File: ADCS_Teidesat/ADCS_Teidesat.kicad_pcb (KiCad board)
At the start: 2 copper layers, 90.2 x 95.9 mm, 10 parts

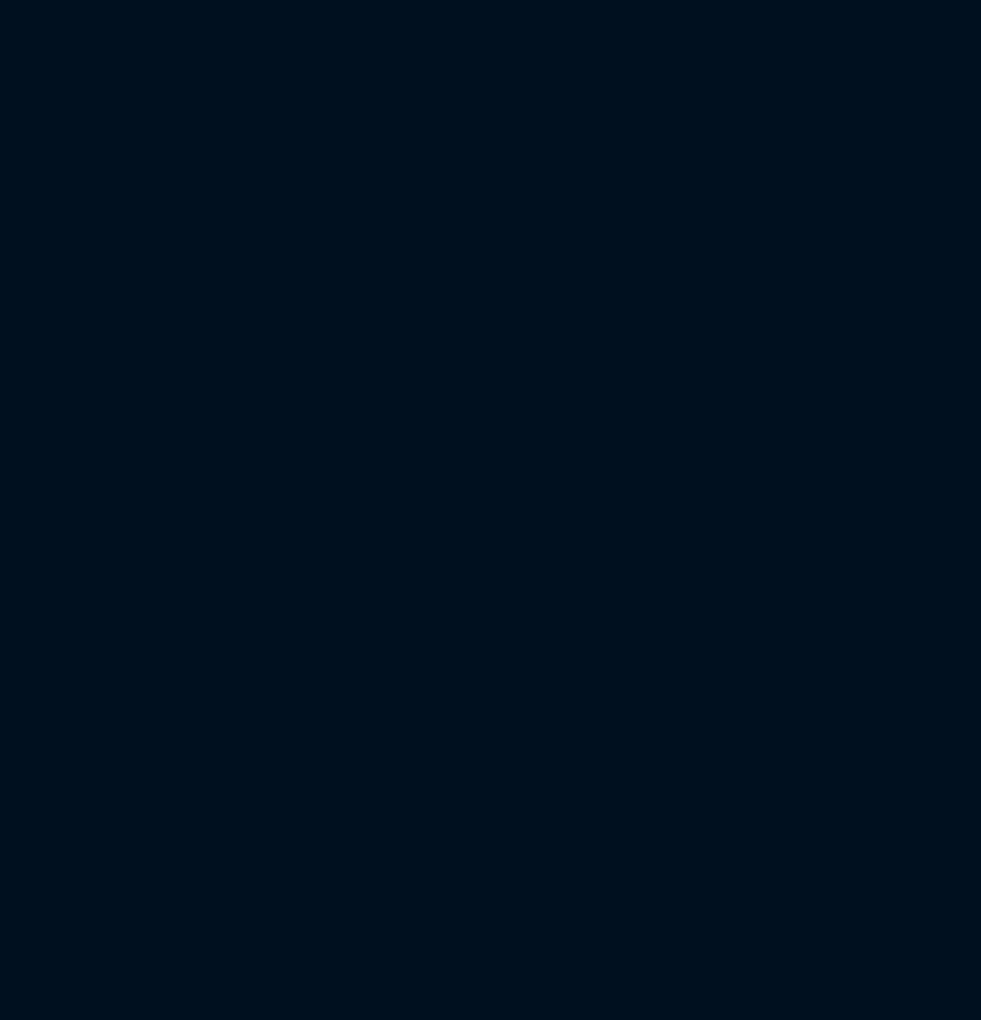
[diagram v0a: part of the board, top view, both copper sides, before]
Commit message: Comienzo PCB
Realizamos los últimos arreglos en las huellas de los componentes y comenzamos el diseño de la PCB

Co-Authored-By: hugohdezmo <238262256+hugohdezmo@users.noreply.github.com>
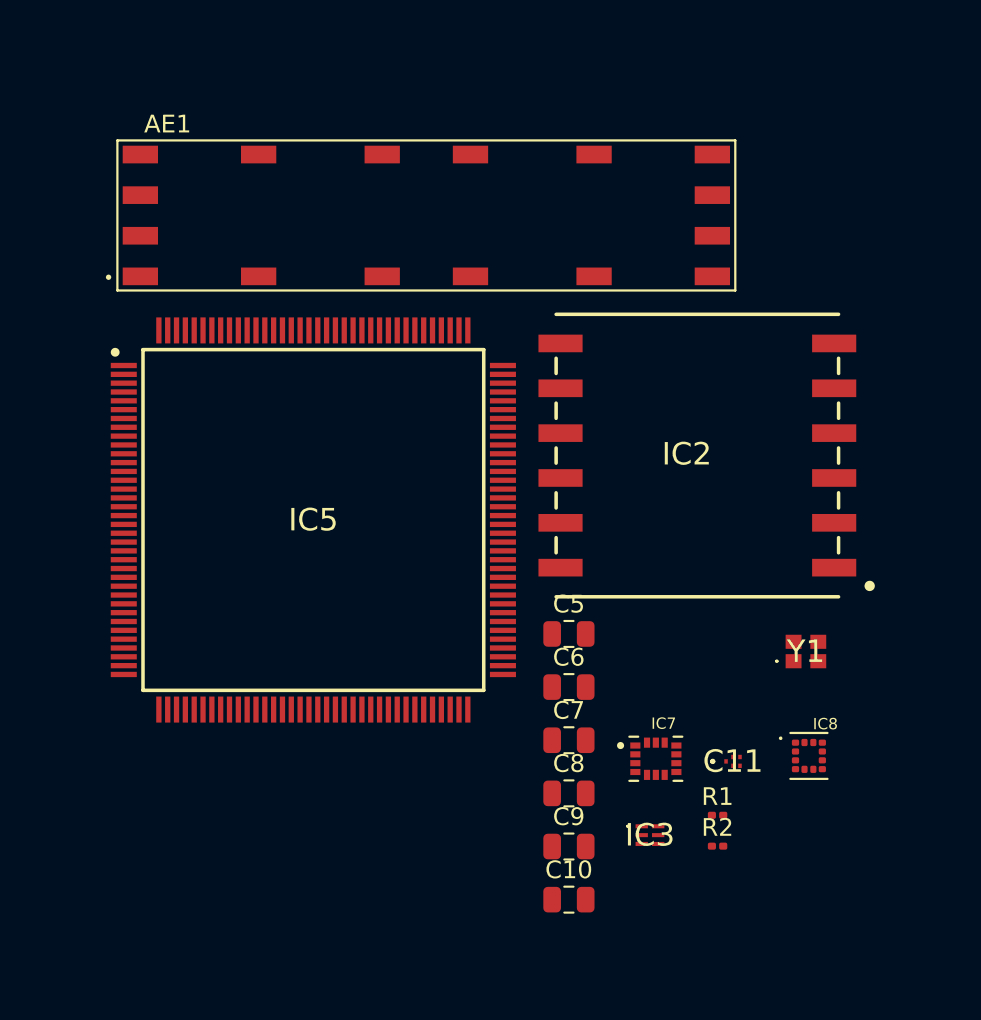
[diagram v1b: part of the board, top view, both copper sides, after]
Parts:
- added AE1: SR4L002, Huellas ADCS:XCVR_SR4L002, F.Cu at (142.1, 83.1)
- added C10: 100n, Capacitor_SMD:C_0805_2012Metric, F.Cu at (150.1, 121.9)
- added C11: F6QA1G581M2QZ-J, Huellas ADCS:F6QA1G581M2QZJ, F.Cu at (159.4, 114.1)
- added C5: 100n, Capacitor_SMD:C_0805_2012Metric, F.Cu at (150.1, 106.8)
- added C6: 100n, Capacitor_SMD:C_0805_2012Metric, F.Cu at (150.1, 109.9)
- added C7: 100n, Capacitor_SMD:C_0805_2012Metric, F.Cu at (150.1, 112.9)
- added C8: 220n, Capacitor_SMD:C_0805_2012Metric, F.Cu at (150.1, 115.9)
- added C9: 100n, Capacitor_SMD:C_0805_2012Metric, F.Cu at (150.1, 118.9)
- added IC2: L86-M33, Huellas ADCS:L80-M39, F.Cu at (149.7, 91.7)
- added IC3: MAX2659ELT+T, Huellas ADCS:MAX2659ELTT, F.Cu at (154.7, 118.2)
- added IC5: TMS5703137DPGEQQ1, Huellas ADCS:QFP50P2200X2200X160-144N, F.Cu at (135.7, 100.4)
- added IC7: LSM6DSV16XTR, Huellas ADCS:XDCR_LSM6DSV16XTR, F.Cu at (155.1, 113.9)
- added IC8: LIS2MDLTR, Huellas ADCS:PQFN50P200X200X70-12N, F.Cu at (163.7, 113.8)
- added R1: 10k, Resistor_SMD:R_0201_0603Metric, F.Cu at (158.6, 117.1)
- added R2: 10k, Resistor_SMD:R_0201_0603Metric, F.Cu at (158.6, 118.9)
- added Y1: ATX-H13-F-16.000MHz-G100-T, Huellas ADCS:ATXH13F16000MHzG100T, F.Cu at (163.6, 107.8)
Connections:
- H1 pad 11: TX2/GP8 -> unconnected-(H1-Pin_11-Pad11)
- H1 pad 13: GP15/A1/RX3 -> unconnected-(H1-Pin_13-Pad13)
- H1 pad 17: GP21/A7/RX5 -> unconnected-(H1-Pin_17-Pad17)
- H1 pad 46: CS/GP10 -> unconnected-(H1-Pin_46-Pad46)
- H1 pad 48: CS/GP37 -> unconnected-(H1-Pin_48-Pad48)
- H1 pad 50: CS/GP36 -> unconnected-(H1-Pin_50-Pad50)
- H1 pad 7: TX1/GP1 -> unconnected-(H1-Pin_7-Pad7)
- H1 pad 9: RX2/GP7 -> unconnected-(H1-Pin_9-Pad9)
- H2 pad 10: SW2 -> unconnected-(H2-Pin_10-Pad10)
- H2 pad 11: SW3 -> unconnected-(H2-Pin_11-Pad11)
- H2 pad 12: SW4 -> unconnected-(H2-Pin_12-Pad12)
- H2 pad 13: SW5 -> unconnected-(H2-Pin_13-Pad13)
- H2 pad 14: SW6 -> unconnected-(H2-Pin_14-Pad14)
- H2 pad 15: SW7 -> unconnected-(H2-Pin_15-Pad15)
- H2 pad 16: SW8 -> unconnected-(H2-Pin_16-Pad16)
- H2 pad 17: SW9 -> unconnected-(H2-Pin_17-Pad17)
- H2 pad 18: SW10 -> unconnected-(H2-Pin_18-Pad18)
- H2 pad 19: SW11 -> unconnected-(H2-Pin_19-Pad19)
- H2 pad 20: SW12 -> unconnected-(H2-Pin_20-Pad20)
- H2 pad 35: PCM_IN -> unconnected-(H2-Pin_35-Pad35)
- H2 pad 41: BCR_OUT -> unconnected-(H2-Pin_41-Pad41)
- H2 pad 43: BCR_OUT -> unconnected-(H2-Pin_43-Pad43)
- H2 pad 44: BCR_OUT -> unconnected-(H2-Pin_44-Pad44)
- H2 pad 9: SW1 -> unconnected-(H2-Pin_9-Pad9)

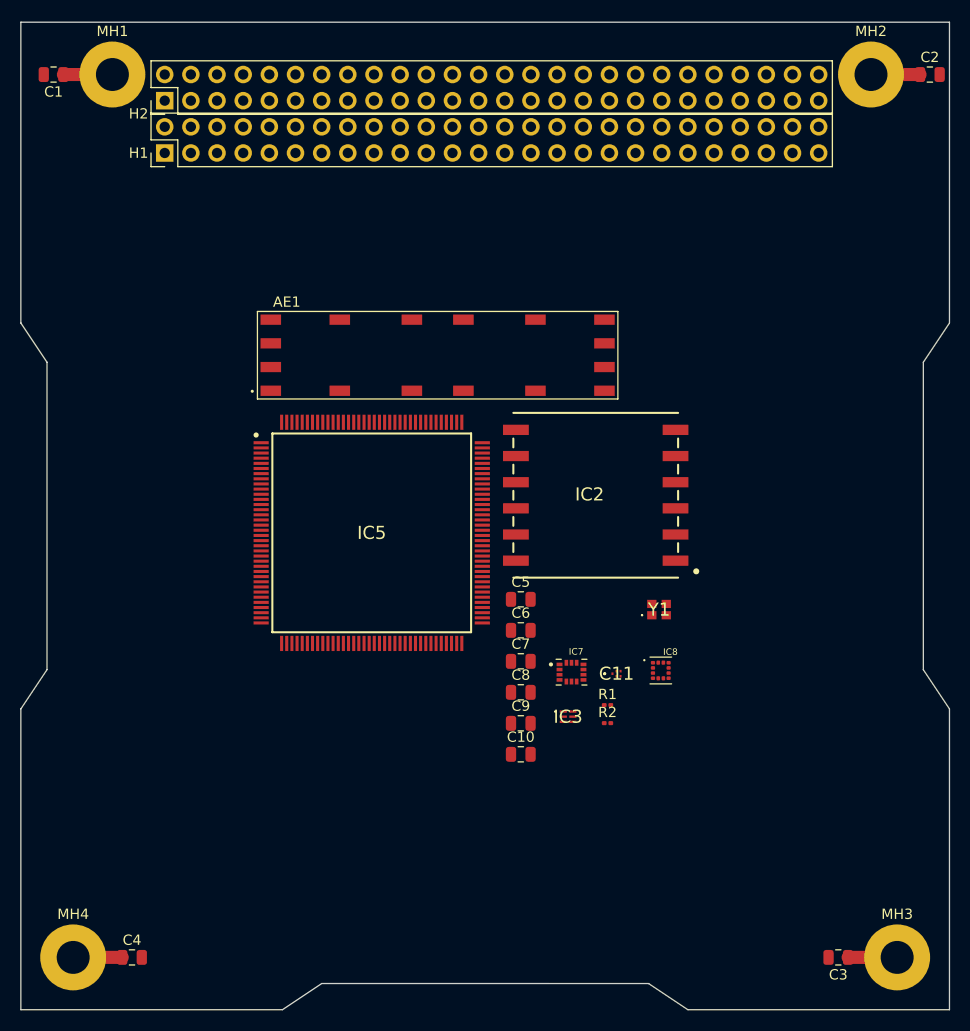
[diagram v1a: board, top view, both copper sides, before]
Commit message: Conexionado de componentes de PCB a falta de revisión
Se ha hecho un primer enrutado de la PCB de la placa ADCS.

Co-Authored-By: Angel-Castro-Vega <236372966+Angel-Castro-Vega@users.noreply.github.com>
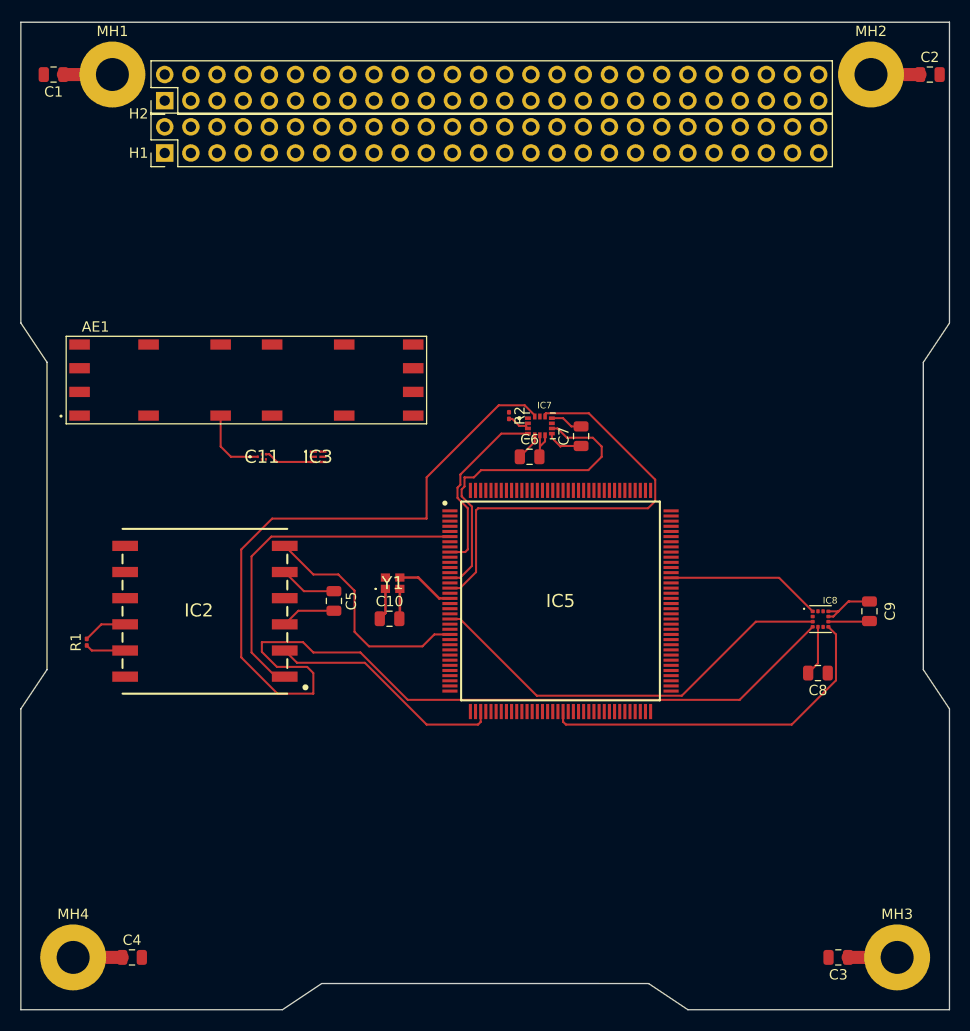
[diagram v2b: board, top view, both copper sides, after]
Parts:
- moved R1 50.9 mm to (108.0, 111.0), turned to 90 degrees
- moved C11 40.4 mm to (125.0, 93.0)
- moved IC2 39.6 mm to (111.7, 102.9)
- moved C9 35.6 mm to (184.0, 108.0), turned to -90 degrees
- moved IC3 35.0 mm to (130.5, 93.0)
- moved R2 31.4 mm to (149.0, 89.0), turned to -90 degrees
- moved C8 28.9 mm to (179.0, 114.0), turned to 180 degrees
- moved Y1 26.0 mm to (137.7, 105.3)
- moved IC7 24.1 mm to (152.0, 90.0)
- moved C7 22.6 mm to (156.0, 91.0), turned to 90 degrees
- moved IC5 19.5 mm to (154.0, 107.0)
- moved AE1 18.7 mm to (123.5, 85.5)
- moved C10 18.3 mm to (137.4, 108.7)
- moved C5 18.1 mm to (132.0, 107.0), turned to -90 degrees
- moved C6 16.9 mm to (151.0, 93.0)
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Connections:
- IC7 pad 4: /INT 1 -> /INT1
- IC7 pad 9: /INT 2 -> /INT2
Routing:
- net /IMU/MAGNETÓMETRO: track 0.00 -> 123.6 mm
- net /CS_IMU: track 0.00 -> 42.7 mm
- net /CS_MAGNETÓMETRO: track 0.00 -> 41.3 mm
- net /INT_MAGNETÓMETRO: track 0.00 -> 34.9 mm
- net /DATA_IN: track 0.00 -> 33.6 mm
- net /INT2: track 0.00 -> 32.5 mm
- net GND: track 0.00 -> 26.1 mm
- net +3V3: track 0.00 -> 24.5 mm
- net /DATA_OUT: track 0.00 -> 23.1 mm
- net /1PPS: track 0.00 -> 22.9 mm
- net /INT1: track 0.00 -> 17.9 mm
- net /SPC_MAG.: track 0.00 -> 15.1 mm
- net /ANTENNA: track 0.00 -> 7.02 mm
- net /OUT_OSC: track 0.00 -> 5.70 mm
- net /RF: track 0.00 -> 4.91 mm
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
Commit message: Arreglo problemas de plantilla
Arreglamos problemas en la plantilla y realizamos ciertas correcciones de Salvador

Co-Authored-By: hugohdezmo <238262256+hugohdezmo@users.noreply.github.com>
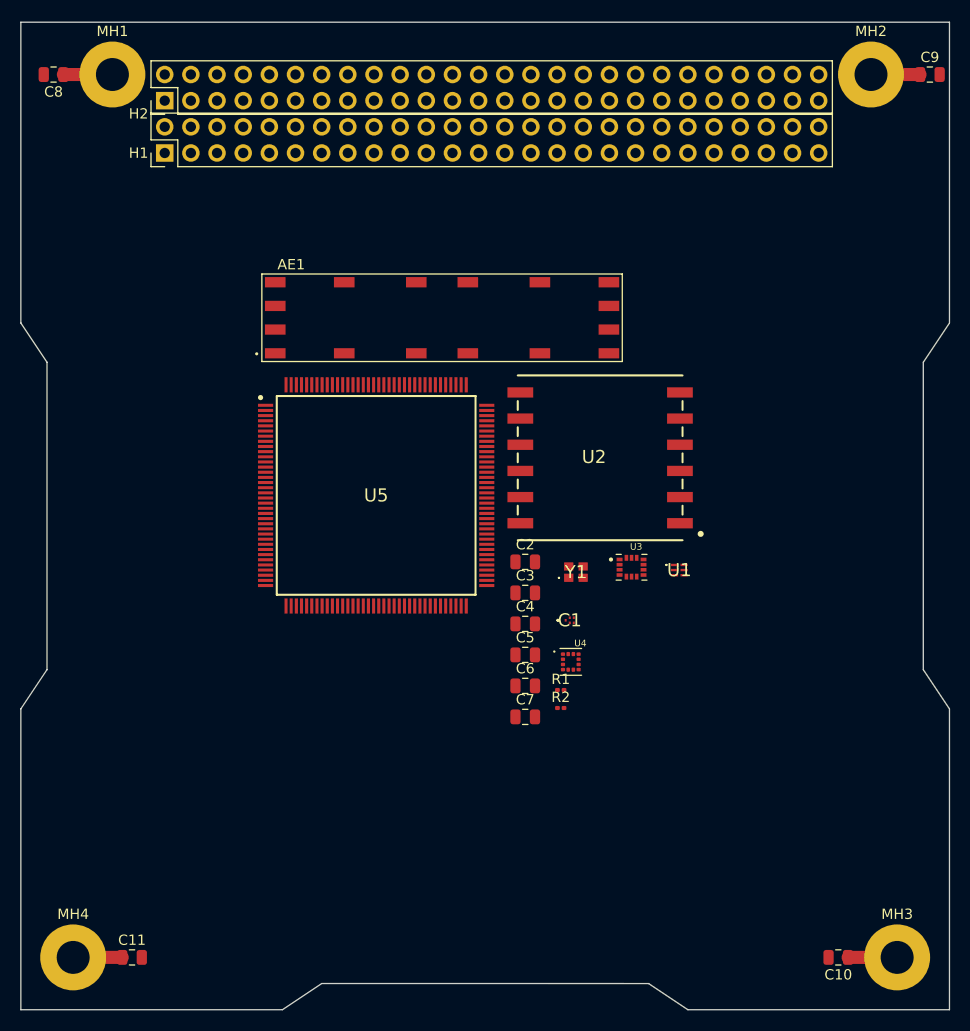
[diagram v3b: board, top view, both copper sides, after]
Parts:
- removed the C10 at (137.4, 108.7)
- removed the C11 at (125.0, 93.0)
- removed the C8 at (179.0, 114.0)
- removed the C9 at (184.0, 108.0)
- removed IC2: L86-M33, Huellas ADCS:L80-M39
- removed IC3: MAX2659ELT+T, Huellas ADCS:MAX2659ELTT
- removed IC5: TMS5703137DPGEQQ1, Huellas ADCS:QFP50P2200X2200X160-144N
- removed IC7: LSM6DSV16XTR, Huellas ADCS:XDCR_LSM6DSV16XTR
- removed IC8: LIS2MDLTR, Huellas ADCS:PQFN50P200X200X70-12N
- added C1: F6QA1G581M2QZ-J, Huellas ADCS:F6QA1G581M2QZJ, F.Cu at (154.9, 108.9)
- added C2: 100n, Capacitor_SMD:C_0805_2012Metric, F.Cu at (150.6, 103.2)
- added C3: 100n, Capacitor_SMD:C_0805_2012Metric, F.Cu at (150.6, 106.2)
- added C4: 100n, Capacitor_SMD:C_0805_2012Metric, F.Cu at (150.6, 109.2)
- added U1: MAX2659ELT+T, Huellas ADCS:MAX2659ELTT, F.Cu at (165.5, 104.0)
- added U2: L86-M33, Huellas ADCS:L80-M39, F.Cu at (150.1, 88.0)
- added U3: LSM6DSV16XTR, Huellas ADCS:XDCR_LSM6DSV16XTR, F.Cu at (160.9, 103.7)
- added U4: LIS2MDLTR, Huellas ADCS:PQFN50P200X200X70-12N, F.Cu at (155.0, 112.9)
- added U5: TMS5703137DPGEQQ1, Huellas ADCS:QFP50P2200X2200X160-144N, F.Cu at (136.1, 96.8)
- C6: value 100n -> 220n
- moved R1 46.3 mm to (154.0, 115.6), turned to 0 degrees
- moved R2 28.8 mm to (154.0, 117.4), turned to 0 degrees
- moved C7 27.8 mm to (150.6, 118.3), turned to 0 degrees
- moved C6 22.2 mm to (150.6, 115.2)
- moved AE1 19.9 mm to (142.5, 79.5)
- moved C5 19.3 mm to (150.6, 112.2), turned to 0 degrees
- moved Y1 17.8 mm to (155.5, 104.2)
- renumbered C3 to C10, C4 to C11, C1 to C8, C2 to C9
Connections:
- C6 pad 1: +3V3 -> GND
- C6 pad 2: GND -> Net-(U4-C1)
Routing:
- net /IMU/MAGNETÓMETRO: track 123.6 -> 0.00 mm
- net /CS_IMU: track 42.7 -> 0.00 mm
- net /CS_MAGNETÓMETRO: track 41.3 -> 0.00 mm
- net /INT_MAGNETÓMETRO: track 34.9 -> 0.00 mm
- net /DATA_IN: track 33.6 -> 0.00 mm
- net /INT2: track 32.5 -> 0.00 mm
- net GND: track 26.1 -> 0.00 mm
- net +3V3: track 24.5 -> 0.00 mm
- net /DATA_OUT: track 23.1 -> 0.00 mm
- net /1PPS: track 22.9 -> 0.00 mm
- net /INT1: track 17.9 -> 0.00 mm
- net /SPC_MAG.: track 15.1 -> 0.00 mm
- net /ANTENNA: track 7.02 -> 0.00 mm
- net /OUT_OSC: track 5.70 -> 0.00 mm
- net /RF: track 4.91 -> 0.00 mm
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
